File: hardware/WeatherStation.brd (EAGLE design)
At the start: 101.3 x 76.2 mm, 9 parts, among them X2 XRJK-S-01-6-4-0-9M2

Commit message: fixing schematic v1.1
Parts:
- removed BMP280: (no value), pinhead:1X06
- removed EXTERN_PINS: (no value), pinhead:1X20
- removed U$1: ESP32DEVKITV1, ESP32-DEVKITV1:ESP32-DEVKITV1
- removed X2: XRJK-S-01-6-4-0-9M2, con-xmultiplee:XRJK-S-01-6-4-0-9M2
- removed XB2: XBEE-PRO, maxstream:XBEE-PRO
- added ESP32: ESP32DEVKITV1, ESP32-DEVKITV1:ESP32-DEVKITV1
- added J2: RJ11, con-rj_fixed:RJ11
- added JP1: (no value), pinhead:1X24
- added ROBOCORE_BEE_V2: XBEE-PRO, maxstream:XBEE-PRO
- moved R3 23.2 mm to (61.0, 55.9)
- moved R2 20.7 mm to (57.1, 55.9), turned to 90 degrees
- moved POWER 11.5 mm to (15.2, 73.7)
- moved R1 10.9 mm to (34.3, 73.7)
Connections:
- removed net N$13: U$1.D16, XB2.2
- removed net N$15: U$1.D5, XB2.5
- new net N$9: ESP32.D22, JP1.21
- net N$1: now also ESP32.3V3, ESP32.D34, J2.3, JP1.1, JP1.11, JP1.17, JP1.5, R3.2, ROBOCORE_BEE_V2.1; no longer POWER.1, U$1.VIN
- net N$10: now also ESP32.D21, JP1.23; no longer BMP280.3, U$1.D22
- net N$11: now also ESP32.D17, ROBOCORE_BEE_V2.3; no longer BMP280.4, U$1.D21
- net N$12: now also J2.2, R2.1; no longer U$1.GND@2, XB2.10
- net N$14: now also J2.1, R3.1; no longer U$1.D17, XB2.3
- net N$2: now also ESP32.D26, ESP32.GND@1, J2.4, JP1.13, JP1.19, JP1.3, JP1.7, R2.2; no longer BMP280.2, EXTERN_PINS.13, EXTERN_PINS.3, EXTERN_PINS.9, R3.2, U$1.D26, U$1.GND@1, X2.1
- net N$3: now also ESP32.D35, R1.1; no longer BMP280.1, EXTERN_PINS.1, EXTERN_PINS.11, EXTERN_PINS.15, EXTERN_PINS.5, R2.1, U$1.3V3, X2.2, XB2.1
- net N$4: now also ESP32.D15, JP1.9; no longer R1.1, U$1.D35
- net N$5: now also ESP32.D16, ROBOCORE_BEE_V2.2; no longer EXTERN_PINS.7, U$1.D15
- net N$6: now also ESP32.GND@2, ROBOCORE_BEE_V2.10; no longer EXTERN_PINS.17, U$1.D4
- net N$7: now also ESP32.D4, JP1.15; no longer R2.2, U$1.D34, X2.4
- net N$8: now also ESP32.VIN, POWER.1; no longer R3.1, X2.3
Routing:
- net N$3: track 348.3 -> 8.54 mm
- net N$1: track 9.73 -> 183.1 mm, vias 0 -> 2
- net N$12: track 11.0 -> 137.4 mm
- net N$5: track 160.2 -> 54.1 mm
- net N$6: track 109.4 -> 13.6 mm
- net N$14: track 51.4 -> 128.8 mm
- net N$7: track 74.6 -> 11.9 mm, vias 0 -> 2
- net N$13: track 54.5 -> 0.00 mm
- net N$10: track 0.00 -> 44.2 mm
- net N$8: track 48.7 -> 8.61 mm
- net N$9: track 0.00 -> 34.5 mm
- net N$15: track 15.1 -> 0.00 mm
- net N$11: track 0.00 -> 14.0 mm
- net N$2: track 236.1 -> 245.1 mm
- net N$4: track 5.17 -> 11.9 mm, vias 0 -> 2
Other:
- board size 101.3 x 76.2 mm -> 79.7 x 80 mm

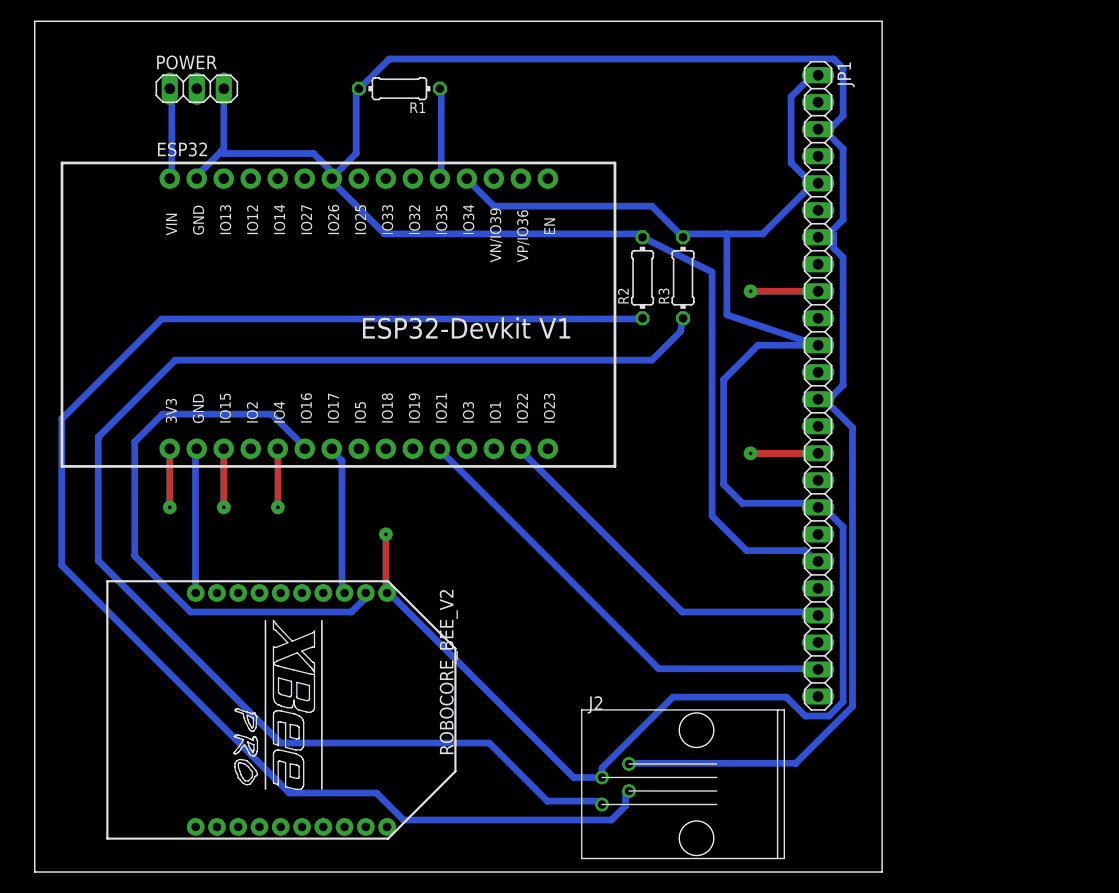
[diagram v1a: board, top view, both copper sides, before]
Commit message: changing rain gauge and wind sensor connection
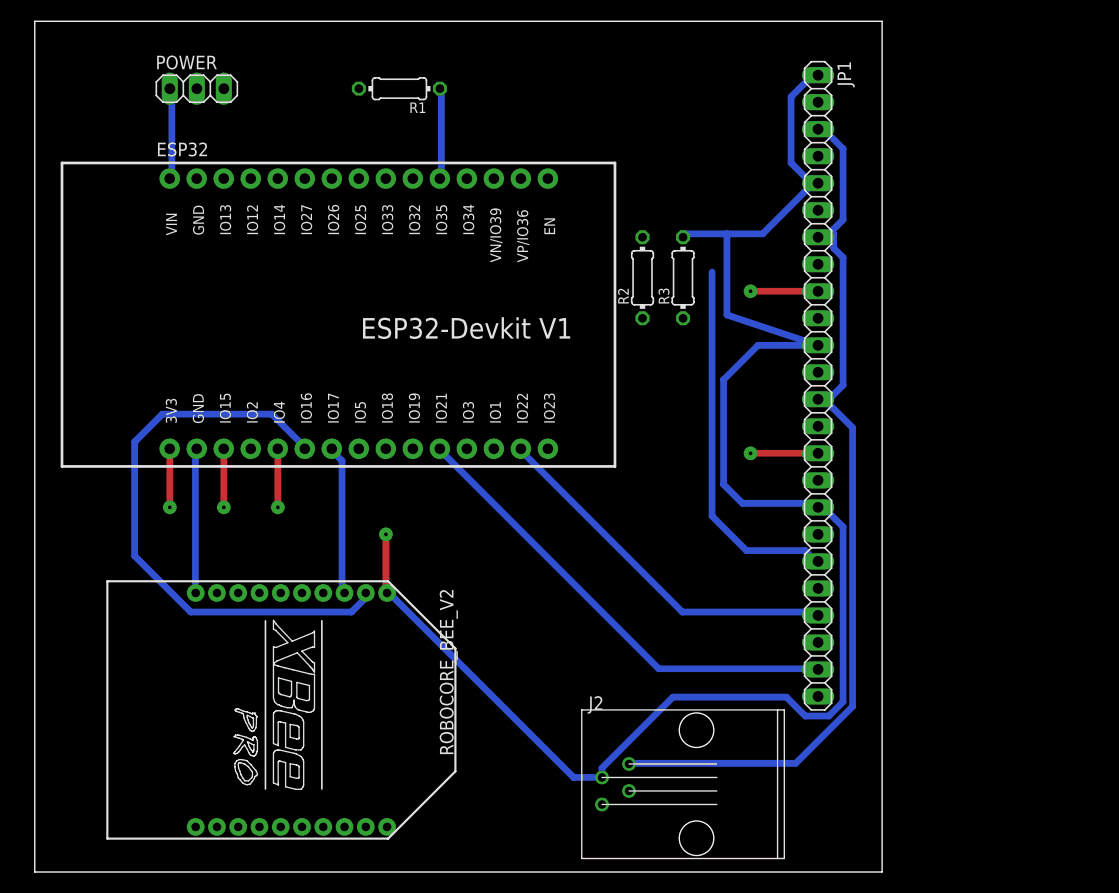
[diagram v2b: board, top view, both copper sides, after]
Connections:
- removed net N$14: J2.1, R3.1
- new net N$13: ESP32.GND@1, J2.4, JP1.13, JP1.19, JP1.7, POWER.3, R1.2, R3.2
- net N$1: now also R2.1; no longer ESP32.D34, R3.2
- net N$12: now also ESP32.D34, R3.1; no longer R2.1
- net N$2: now also J2.1; no longer ESP32.GND@1, J2.4, JP1.13, JP1.19, JP1.3, JP1.7, POWER.3, R1.2
- net N$3: now also JP1.3
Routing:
- net N$2: track 245.1 -> 0.00 mm
- net N$12: track 137.4 -> 0.00 mm
- net N$14: track 128.8 -> 0.00 mm
- net N$13: track 0.00 -> 120.4 mm
- net N$1: track 183.1 -> 160.1 mm
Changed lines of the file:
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@@
 <wire x1="38.227" y1="73.3425" x2="38.1" y2="73.66" width="0.635" layer="16"/>
 <wire x1="38.227" y1="65.3415" x2="38.09" y2="65.205" width="0.635" layer="16"/>
+<contactref element="JP1" pad="3"/>
+<wire x1="38.1" y1="73.66" x2="73.66" y2="69.85" width="0" layer="19" extent="1-1"/>
 </signal>
 <signal name="N$4">
@@
 <contactref element="JP1" pad="17"/>
 <contactref element="ESP32" pad="3V3"/>
-<contactref element="R3" pad="2"/>
-<contactref element="ESP32" pad="D34"/>
 <contactref element="J2" pad="3"/>
 <wire x1="50.673" y1="8.89" x2="53.34" y2="8.89" width="0.635" layer="16"/>
@@
 <wire x1="65.0875" y1="60.0075" x2="61.087" y2="60.0075" width="0.635" layer="16"/>
 <wire x1="73.3425" y1="64.897" x2="68.453" y2="60.0075" width="0.635" layer="16"/>
-<wire x1="61.087" y1="60.0075" x2="60.96" y2="59.69" width="0.635" layer="16"/>
 <wire x1="73.3425" y1="64.897" x2="73.66" y2="64.77" width="0.635" layer="16"/>
 <wire x1="72.898" y1="74.676" x2="73.3425" y2="74.676" width="0.635" layer="16"/>
@@
 <wire x1="73.3425" y1="74.676" x2="73.66" y2="74.93" width="0.635" layer="16"/>
 <wire x1="72.898" y1="64.897" x2="73.66" y2="64.77" width="0.635" layer="16"/>
-<wire x1="43.18" y1="62.611" x2="40.894" y2="64.897" width="0.635" layer="16"/>
-<wire x1="58.039" y1="62.611" x2="43.18" y2="62.611" width="0.635" layer="16"/>
-<wire x1="60.96" y1="59.69" x2="58.039" y2="62.611" width="0.635" layer="16"/>
-<wire x1="40.894" y1="64.897" x2="40.63" y2="65.205" width="0.635" layer="16"/>
 <wire x1="65.0875" y1="60.0075" x2="65.0875" y2="52.3875" width="0.635" layer="16"/>
 <wire x1="65.0875" y1="52.3875" x2="73.66" y2="49.53" width="0.635" layer="16"/>
@@
 <via x="12.7" y="34.29" extent="1-16" drill="0.35" diameter="1.3"/>
 <via x="33.02" y="31.75" extent="1-16" drill="0.35" diameter="1.3"/>
+<contactref element="R2" pad="1"/>
+<wire x1="61.087" y1="60.0075" x2="57.15" y2="52.07" width="0" layer="19" extent="16-16"/>
 <wire x1="12.7" y1="34.29" x2="33.02" y2="31.75" width="0" layer="19" extent="1-1"/>
 </signal>
@@
 <wire x1="28.0035" y1="39.5605" x2="27.93" y2="39.8" width="0.635" layer="16"/>
 </signal>
-<signal name="N$12">
-<contactref element="R2" pad="1"/>
-<contactref element="J2" pad="2"/>
-<wire x1="55.5625" y1="6.223" x2="55.5625" y2="7.5565" width="0.635" layer="16"/>
-<wire x1="54.229" y1="4.8895" x2="55.5625" y2="6.223" width="0.635" layer="16"/>
-<wire x1="34.671" y1="4.8895" x2="54.229" y2="4.8895" width="0.635" layer="16"/>
-<wire x1="32.131" y1="7.4295" x2="34.671" y2="4.8895" width="0.635" layer="16"/>
-<wire x1="23.9395" y1="7.4295" x2="32.131" y2="7.4295" width="0.635" layer="16"/>
-<wire x1="2.54" y1="28.829" x2="23.9395" y2="7.4295" width="0.635" layer="16"/>
-<wire x1="2.54" y1="42.6085" x2="2.54" y2="28.829" width="0.635" layer="16"/>
-<wire x1="11.938" y1="52.0065" x2="2.54" y2="42.6085" width="0.635" layer="16"/>
-<wire x1="56.9595" y1="52.0065" x2="11.938" y2="52.0065" width="0.635" layer="16"/>
-<wire x1="55.5625" y1="7.5565" x2="55.88" y2="7.62" width="0.635" layer="16"/>
-<wire x1="56.9595" y1="52.0065" x2="57.15" y2="52.07" width="0.635" layer="16"/>
-</signal>
-<signal name="N$2">
-<contactref element="R2" pad="2"/>
-<contactref element="ESP32" pad="D26"/>
+<signal name="N$13">
 <contactref element="POWER" pad="3"/>
 <contactref element="ESP32" pad="GND@1"/>
-<contactref element="JP1" pad="3"/>
 <contactref element="R1" pad="2"/>
 <contactref element="JP1" pad="7"/>
@@
 <wire x1="73.787" y1="70.231" x2="76.0095" y2="68.0085" width="0.635" layer="16"/>
 <wire x1="73.787" y1="60.0075" x2="73.66" y2="59.69" width="0.635" layer="16"/>
-<wire x1="73.787" y1="70.231" x2="73.66" y2="69.85" width="0.635" layer="16"/>
 <wire x1="71.5645" y1="10.2235" x2="56.007" y2="10.2235" width="0.635" layer="16"/>
 <wire x1="76.8985" y1="15.5575" x2="71.5645" y2="10.2235" width="0.635" layer="16"/>
@@
 <wire x1="75.1205" y1="60.0075" x2="73.66" y2="59.69" width="0.635" layer="16"/>
 <wire x1="74.676" y1="44.45" x2="73.66" y2="44.45" width="0.635" layer="16"/>
-<wire x1="17.78" y1="68.0085" x2="17.78" y2="73.66" width="0.635" layer="16"/>
-<wire x1="15.113" y1="65.3415" x2="17.55775" y2="67.78625" width="0.635" layer="16"/>
-<wire x1="17.55775" y1="67.78625" x2="17.78" y2="68.0085" width="0.635" layer="16"/>
-<wire x1="15.113" y1="65.3415" x2="15.23" y2="65.205" width="0.635" layer="16"/>
-<wire x1="32.893" y1="60.0075" x2="56.9595" y2="60.0075" width="0.635" layer="16"/>
-<wire x1="28.0035" y1="64.897" x2="32.893" y2="60.0075" width="0.635" layer="16"/>
-<wire x1="56.9595" y1="60.0075" x2="57.15" y2="59.69" width="0.635" layer="16"/>
-<wire x1="28.0035" y1="64.897" x2="27.93" y2="65.205" width="0.635" layer="16"/>
-<wire x1="30.226" y1="67.564" x2="30.226" y2="73.3425" width="0.635" layer="16"/>
-<wire x1="28.0035" y1="65.3415" x2="30.226" y2="67.564" width="0.635" layer="16"/>
-<wire x1="30.226" y1="73.3425" x2="30.48" y2="73.66" width="0.635" layer="16"/>
-<wire x1="28.0035" y1="65.3415" x2="27.93" y2="65.205" width="0.635" layer="16"/>
 <wire x1="72.4535" y1="30.226" x2="73.3425" y2="29.337" width="0.635" layer="16"/>
 <wire x1="66.929" y1="30.226" x2="72.4535" y2="30.226" width="0.635" layer="16"/>
@@
 <wire x1="63.6905" y1="56.41975" x2="63.6905" y2="33.4645" width="0.635" layer="16"/>
 <wire x1="73.3425" y1="29.337" x2="73.66" y2="29.21" width="0.635" layer="16"/>
-<wire x1="63.6905" y1="56.41975" x2="57.15" y2="59.69" width="0.635" layer="16"/>
-<wire x1="26.2255" y1="67.564" x2="17.78" y2="67.564" width="0.635" layer="16"/>
-<wire x1="28.0035" y1="65.786" x2="26.2255" y2="67.564" width="0.635" layer="16"/>
-<wire x1="17.78" y1="67.564" x2="17.55775" y2="67.78625" width="0.635" layer="16"/>
-<wire x1="28.0035" y1="65.786" x2="27.93" y2="65.205" width="0.635" layer="16"/>
-<wire x1="76.0095" y1="71.12" x2="74.676" y2="69.7865" width="0.635" layer="16"/>
-<wire x1="76.0095" y1="75.565" x2="76.0095" y2="71.12" width="0.635" layer="16"/>
-<wire x1="75.1205" y1="76.454" x2="76.0095" y2="75.565" width="0.635" layer="16"/>
-<wire x1="33.3375" y1="76.454" x2="75.1205" y2="76.454" width="0.635" layer="16"/>
-<wire x1="30.6705" y1="73.787" x2="33.3375" y2="76.454" width="0.635" layer="16"/>
-<wire x1="74.676" y1="69.7865" x2="73.66" y2="69.85" width="0.635" layer="16"/>
-<wire x1="30.6705" y1="73.787" x2="30.48" y2="73.66" width="0.635" layer="16"/>
+<contactref element="R3" pad="2"/>
+<wire x1="63.6905" y1="56.41975" x2="60.96" y2="59.69" width="0" layer="19" extent="16-16"/>
+<wire x1="73.66" y1="59.69" x2="63.6905" y2="56.41975" width="0" layer="19" extent="16-16"/>
+<wire x1="30.48" y1="73.66" x2="60.96" y2="59.69" width="0" layer="19" extent="1-1"/>
+<wire x1="17.78" y1="73.66" x2="30.48" y2="73.66" width="0" layer="19" extent="1-1"/>
+<wire x1="15.23" y1="65.205" x2="17.78" y2="73.66" width="0" layer="19" extent="1-1"/>
 </signal>
-<signal name="N$14">
+<signal name="N$2">
+<contactref element="ESP32" pad="D26"/>
+<contactref element="J2" pad="1"/>
+<contactref element="R2" pad="2"/>
+<wire x1="27.93" y1="65.205" x2="57.15" y2="59.69" width="0" layer="19" extent="1-1"/>
+<wire x1="53.34" y1="6.35" x2="57.15" y2="59.69" width="0" layer="19" extent="1-1"/>
+</signal>
+<signal name="N$12">
+<contactref element="ESP32" pad="D34"/>
+<contactref element="J2" pad="2"/>
 <contactref element="R3" pad="1"/>
-<contactref element="J2" pad="1"/>
-<wire x1="48.1965" y1="6.6675" x2="53.34" y2="6.6675" width="0.635" layer="16"/>
-<wire x1="42.7355" y1="12.1285" x2="48.1965" y2="6.6675" width="0.635" layer="16"/>
-<wire x1="23.114" y1="12.1285" x2="42.7355" y2="12.1285" width="0.635" layer="16"/>
-<wire x1="5.969" y1="29.2735" x2="23.114" y2="12.1285" width="0.635" layer="16"/>
-<wire x1="5.969" y1="40.894" x2="5.969" y2="29.2735" width="0.635" layer="16"/>
-<wire x1="13.208" y1="48.133" x2="5.969" y2="40.894" width="0.635" layer="16"/>
-<wire x1="58.039" y1="48.133" x2="13.208" y2="48.133" width="0.635" layer="16"/>
-<wire x1="60.706" y1="50.8" x2="58.039" y2="48.133" width="0.635" layer="16"/>
-<wire x1="53.34" y1="6.6675" x2="53.34" y2="6.35" width="0.635" layer="16"/>
-<wire x1="60.706" y1="50.8" x2="60.96" y2="52.07" width="0.635" layer="16"/>
+<wire x1="40.63" y1="65.205" x2="60.96" y2="52.07" width="0" layer="19" extent="1-1"/>
+<wire x1="55.88" y1="7.62" x2="60.96" y2="52.07" width="0" layer="19" extent="1-1"/>
 </signal>
 </signals>

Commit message: updating schematic, better board, and portuguese fzz
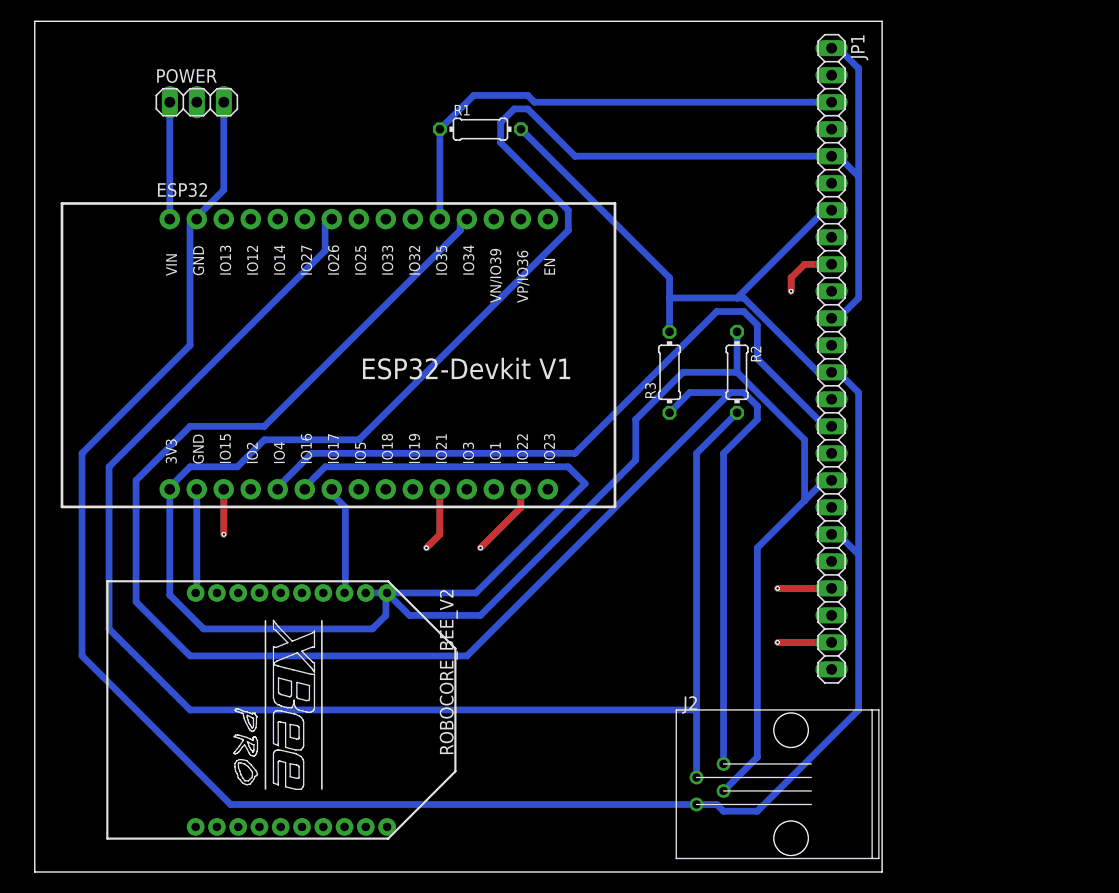
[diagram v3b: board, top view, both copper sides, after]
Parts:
- moved R2 12.6 mm to (66.0, 47.0), turned to 270 degrees
- moved R3 8.98 mm to (59.7, 47.0)
- moved J2 8.89 mm to (68.6, 8.89)
- moved R1 8.52 mm to (41.9, 69.8), turned to 0 degrees
- moved ESP32 3.81 mm to (29.2, 48.3)
- moved JP1 2.84 mm to (74.9, 48.3)
- moved POWER 1.27 mm to (15.2, 72.4)
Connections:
- removed net N$12: ESP32.D34, J2.2, R3.1
- new net N$16: ESP32.D34, J2.4, R3.1
- net N$1: now also J2.2; no longer J2.3
- net N$13: now also J2.1; no longer J2.4
- net N$2: now also J2.3; no longer J2.1
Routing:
- net N$16: track 0.00 -> 165.8 mm
- net N$2: track 0.00 -> 141.5 mm
- net N$13: track 120.4 -> 232.5 mm
- net N$1: track 160.1 -> 257.5 mm, vias 2 -> 0
- net N$7: track 11.9 -> 65.4 mm, vias 2 -> 0
- net N$3: track 8.54 -> 46.9 mm
- net N$10: track 44.2 -> 11.1 mm
- net N$9: track 34.5 -> 12.2 mm
- net N$6: track 13.6 -> 9.76 mm
- net N$11: track 14.0 -> 10.3 mm
- net N$8: track 8.61 -> 11.0 mm
- net N$4: track 11.9 -> 9.85 mm, vias 2 -> 0
- net N$5: track 54.1 -> 52.9 mm
